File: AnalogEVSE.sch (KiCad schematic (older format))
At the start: 64 parts, among them K1 Relay, P1 230V, P2 Relay 2, P3 Relay 1, P4 Pilot, P5 Status LEDs, P6 Rext, P7 Power, Q1 BC337, Q2 BC557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

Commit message: Release 2.0.3
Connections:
- net +12V: now also K1.9, U5.3 (V+), U5.3 (V+), U5.3 (V+); no longer K1.8
- net -12V: now also U3.12 (GND), U3.12 (GND), U3.12 (GND), U5.12 (GND), U5.12 (GND), U5.12 (GND)
- net at C6.2, D3.1 (A), Q3.3 (C): now also K1.8; no longer K1.9
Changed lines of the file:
@@
 EESchema Schematic File Version 4
 LIBS:AnalogEVSE-cache
-EELAYER 26 0
+EELAYER 29 0
 EELAYER END
 $Descr A4 11693 8268
 encoding utf-8
 Sheet 1 1
-Title "AnalogEVSE 2.0.0"
-Date "2019-03-07"
-Rev "2.0.0"
+Title "AnalogEVSE"
+Date "2019-12-21"
+Rev "2.0.3"
 Comp ""
 Comment1 "Analog J1772 charge controller"
@@
 Connection ~ 1850 4750
 Wire Wire Line
-	9400 1650 9300 1650
-Wire Wire Line
 	7400 3050 7600 3050
 Connection ~ 9300 1950
@@
 	9300 2950 9300 2850
 Wire Wire Line
-	9300 1650 9300 1950
+	9300 1550 9300 1950
 Wire Wire Line
 	9300 2500 9300 2450
@@
 	9050 1950 9300 1950
 Wire Wire Line
-	9050 1550 9400 1550
-Wire Wire Line
 	1850 3550 1950 3550
 Wire Wire Line
@@
 Wire Notes Line
 	800  5750 1250 5750
+Wire Wire Line
+	9300 1550 9400 1550
+Wire Wire Line
+	9400 1650 9200 1650
+Wire Wire Line
+	9200 1650 9200 1550
+Wire Wire Line
+	9200 1550 9050 1550
+$Comp
+L power:+12V #PWR0104
+U 1 1 5CF52CE3
+P 2750 5350
+F 0 "#PWR0104" H 2750 5300 20  0001 C CNN
+F 1 "+12V" H 2850 5450 30  0000 C CNN
+F 2 "" H 2750 5350 60  0000 C CNN
+F 3 "" H 2750 5350 60  0000 C CNN
+	1    2750 5350
+	1    0    0    -1
+$EndComp
+$Comp
+L power:+12V #PWR0105
+U 1 1 5CF54778
+P 2750 6350
+F 0 "#PWR0105" H 2750 6300 20  0001 C CNN
+F 1 "+12V" H 2850 6450 30  0000 C CNN
+F 2 "" H 2750 6350 60  0000 C CNN
+F 3 "" H 2750 6350 60  0000 C CNN
+	1    2750 6350
+	1    0    0    -1
+$EndComp
+$Comp
+L power:+12V #PWR0106
+U 1 1 5CF54C3A
+P 8400 2650
+F 0 "#PWR0106" H 8400 2600 20  0001 C CNN
+F 1 "+12V" H 8500 2750 30  0000 C CNN
+F 2 "" H 8400 2650 60  0000 C CNN
+F 3 "" H 8400 2650 60  0000 C CNN
+	1    8400 2650
+	1    0    0    -1
+$EndComp
+$Comp
+L power:-12V #PWR0107
+U 1 1 5CF559ED
+P 2750 5950
+F 0 "#PWR0107" H 2750 6080 20  0001 C CNN
+F 1 "-12V" H 2750 6050 30  0000 C CNN
+F 2 "" H 2750 5950 60  0000 C CNN
+F 3 "" H 2750 5950 60  0000 C CNN
+	1    2750 5950
+	-1   0    0    1
+$EndComp
+$Comp
+L power:-12V #PWR0108
+U 1 1 5CF560EB
+P 2750 6950
+F 0 "#PWR0108" H 2750 7080 20  0001 C CNN
+F 1 "-12V" H 2750 7050 30  0000 C CNN
+F 2 "" H 2750 6950 60  0000 C CNN
+F 3 "" H 2750 6950 60  0000 C CNN
+	1    2750 6950
+	-1   0    0    1
+$EndComp
+$Comp
+L power:-12V #PWR0109
+U 1 1 5CF56610
+P 6950 4200
+F 0 "#PWR0109" H 6950 4330 20  0001 C CNN
+F 1 "-12V" H 6950 4300 30  0000 C CNN
+F 2 "" H 6950 4200 60  0000 C CNN
+F 3 "" H 6950 4200 60  0000 C CNN
+	1    6950 4200
+	-1   0    0    1
+$EndComp
+$Comp
+L power:-12V #PWR0110
+U 1 1 5CF56BDF
+P 6950 5050
+F 0 "#PWR0110" H 6950 5180 20  0001 C CNN
+F 1 "-12V" H 6950 5150 30  0000 C CNN
+F 2 "" H 6950 5050 60  0000 C CNN
+F 3 "" H 6950 5050 60  0000 C CNN
+	1    6950 5050
+	-1   0    0    1
+$EndComp
+$Comp
+L power:-12V #PWR0111
+U 1 1 5CF572AD
+P 6950 5900
+F 0 "#PWR0111" H 6950 6030 20  0001 C CNN
+F 1 "-12V" H 6950 6000 30  0000 C CNN
+F 2 "" H 6950 5900 60  0000 C CNN
+F 3 "" H 6950 5900 60  0000 C CNN
+	1    6950 5900
+	-1   0    0    1
+$EndComp
+$Comp
+L power:-12V #PWR0112
+U 1 1 5CF57B0F
+P 8400 3250
+F 0 "#PWR0112" H 8400 3380 20  0001 C CNN
+F 1 "-12V" H 8400 3350 30  0000 C CNN
+F 2 "" H 8400 3250 60  0000 C CNN
+F 3 "" H 8400 3250 60  0000 C CNN
+	1    8400 3250
+	-1   0    0    1
+$EndComp
 $EndSCHEMATC

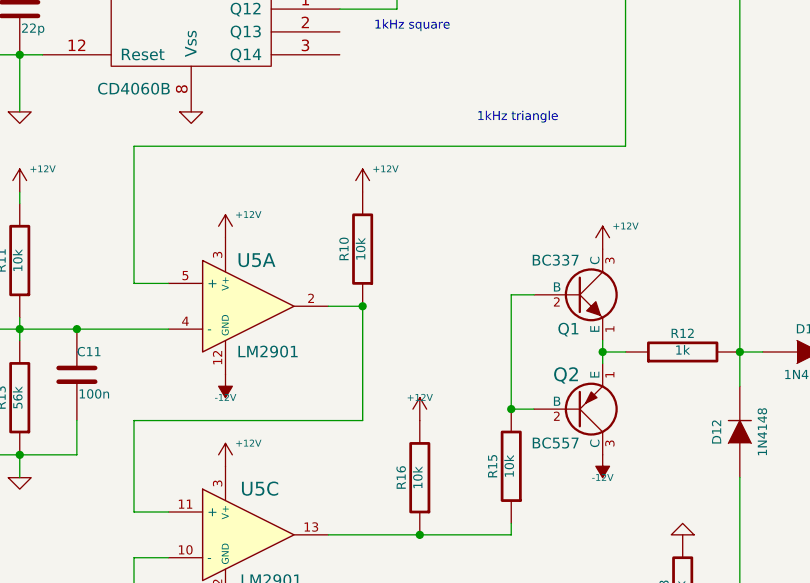
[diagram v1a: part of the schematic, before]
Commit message: Version 2.0.4 with R20 for proper +12V when idle
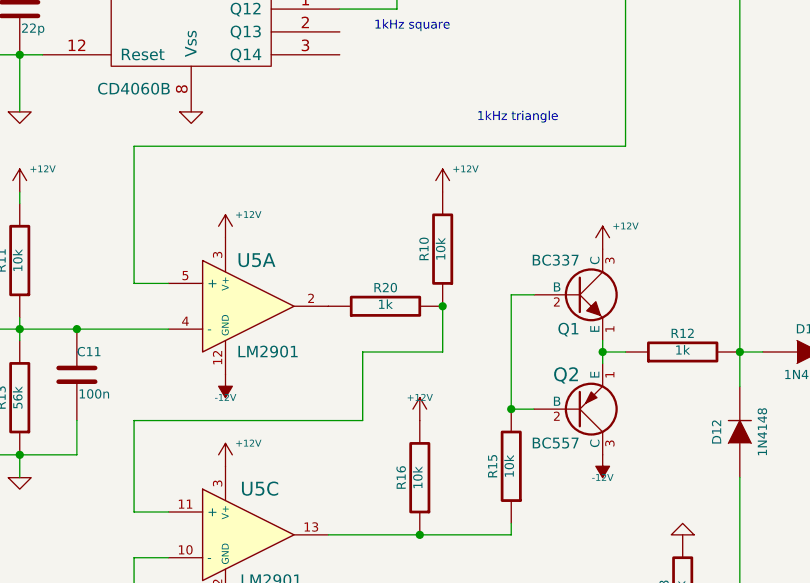
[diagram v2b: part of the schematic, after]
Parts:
- added R20: 1k, mylib:R3.5, symbol AnalogEVSE-rescue:R-RESCUE-AnalogEVSE
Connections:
- net at R10.1, U5.11 (+): now also R20.2; no longer U5.2
- new net: R20.1, U5.2
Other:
- moved on the sheet: R10
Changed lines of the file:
@@
 EESchema Schematic File Version 4
-LIBS:AnalogEVSE-cache
-EELAYER 29 0
+EELAYER 30 0
 EELAYER END
 $Descr A4 11693 8268
@@
 Sheet 1 1
 Title "AnalogEVSE"
-Date "2019-12-21"
-Rev "2.0.3"
+Date "2021-07-11"
+Rev "2.0.4"
 Comp ""
 Comment1 "Analog J1772 charge controller"
@@
 L AnalogEVSE-rescue:R-RESCUE-AnalogEVSE R10
 U 1 1 564853D7
-P 3350 4400
-F 0 "R10" V 3430 4400 40  0000 C CNN
-F 1 "10k" V 3357 4401 40  0000 C CNN
-F 2 "mylib:R3.5" V 3280 4400 30  0001 C CNN
-F 3 "~" H 3350 4400 30  0000 C CNN
-	1    3350 4400
+P 3700 4400
+F 0 "R10" V 3780 4400 40  0000 C CNN
+F 1 "10k" V 3707 4401 40  0000 C CNN
+F 2 "mylib:R3.5" V 3630 4400 30  0001 C CNN
+F 3 "~" H 3700 4400 30  0000 C CNN
+	1    3700 4400
 	-1   0    0    1
 $EndComp
@@
 L power:+12V #PWR07
 U 1 1 564853DE
-P 3350 4150
-F 0 "#PWR07" H 3350 4100 20  0001 C CNN
-F 1 "+12V" H 3450 4250 30  0000 C CNN
-F 2 "" H 3350 4150 60  0000 C CNN
-F 3 "" H 3350 4150 60  0000 C CNN
-	1    3350 4150
+P 3700 4150
+F 0 "#PWR07" H 3700 4100 20  0001 C CNN
+F 1 "+12V" H 3800 4250 30  0000 C CNN
+F 2 "" H 3700 4150 60  0000 C CNN
+F 3 "" H 3700 4150 60  0000 C CNN
+	1    3700 4150
 	1    0    0    -1
 $EndComp
@@
 $EndComp
 Wire Wire Line
-	3200 4650 3350 4650
-Wire Wire Line
 	2350 5550 2500 5550
 Wire Wire Line
@@
 	1750 800  2100 800
 Connection ~ 9050 1950
-Connection ~ 3350 4650
 Connection ~ 5000 7000
 Connection ~ 4750 7500
@@
 	9050 1450 9050 1550
 Connection ~ 5500 5350
-Wire Wire Line
-	3350 4650 3350 5150
 Wire Wire Line
 	2500 5750 2350 5750
@@
 	-1   0    0    1
 $EndComp
+$Comp
+L AnalogEVSE-rescue:R-RESCUE-AnalogEVSE R20
+U 1 1 60EC0875
+P 3450 4650
+F 0 "R20" V 3530 4650 40  0000 C CNN
+F 1 "1k" V 3457 4651 40  0000 C CNN
+F 2 "mylib:R3.5" V 3380 4650 30  0001 C CNN
+F 3 "~" H 3450 4650 30  0000 C CNN
+	1    3450 4650
+	0    -1   -1   0
+$EndComp
+Wire Wire Line
+	3700 4650 3700 4850
+Wire Wire Line
+	3700 4850 3350 4850
+Wire Wire Line
+	3350 4850 3350 5150
+Connection ~ 3700 4650
 $EndSCHEMATC
